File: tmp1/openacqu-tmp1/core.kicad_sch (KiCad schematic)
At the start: 35 parts, among them J1 GSB1C41110SSHR, J2 Test Points, U1 MCP2221AT-I_ML, U2 LP5817DRLR, U3 FXL6408UMX, U4 24AA025E48T-E_OT, U5 AP2112K-3.3TRG1, U6 TPS22996HQDYCRQ1

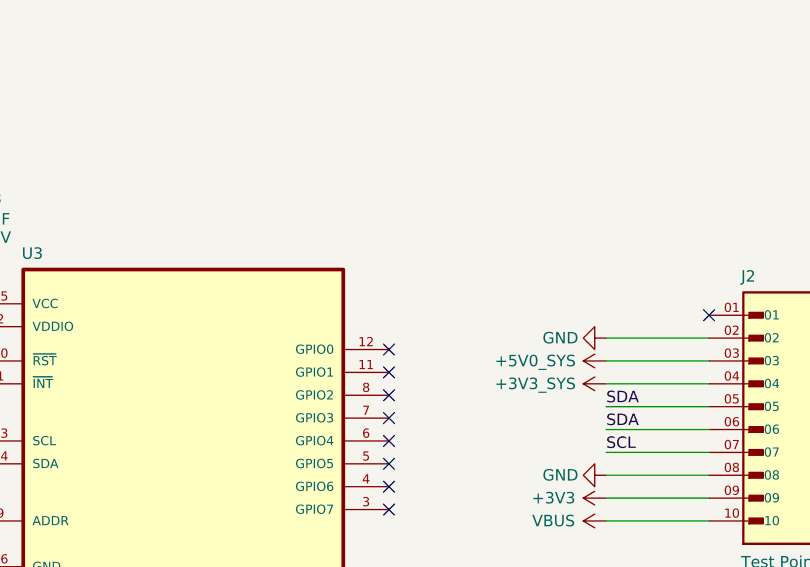
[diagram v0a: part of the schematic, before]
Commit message: Completed layout for the TMP1
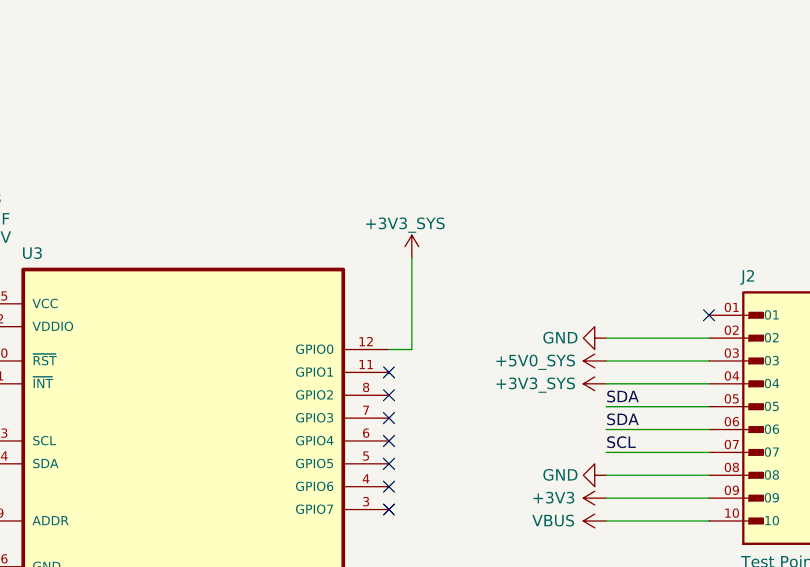
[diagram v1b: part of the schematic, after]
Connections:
- net +3V3_SYS: now also U3.12 (GPIO0)
- no-connect marks 19 -> 18
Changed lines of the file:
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@@
 	)
 	(no_connect
-		(at 229.87 110.49)
-	)
-	(no_connect
 		(at 69.85 124.46)
 	)
@@
 	(wire
 		(pts
+			(xy 232.41 110.49) (xy 229.87 110.49)
+		)
+		(stroke
+			(width 0)
+			(type default)
+		)
+	)
+	(wire
+		(pts
 			(xy 31.75 165.1) (xy 31.75 152.4)
 		)
@@
 	(wire
 		(pts
+			(xy 232.41 110.49) (xy 232.41 100.33)
+		)
+		(stroke
+			(width 0)
+			(type default)
+		)
+	)
+	(wire
+		(pts
 			(xy 168.91 111.76) (xy 168.91 114.3)
 		)
@@
 					(unit 1)
 				)
+			)
+		)
+	)
+	(symbol
+		(lib_id "power:+3V3")
+		(at 232.41 100.33 0)
+		(unit 1)
+		(exclude_from_sim no)
+		(in_bom yes)
+		(on_board yes)
+		(dnp no)
+		(property "Reference" "#PWR047"
+			(at 232.41 104.14 0)
+			(effects
+				(font
+					(size 1.27 1.27)
+				)
+				(hide yes)
+			)
+		)
+		(property "Value" "+3V3_SYS"
+			(at 231.648 96.52 0)
+			(effects
+				(font
+					(size 1.27 1.27)
+				)
+			)
+		)
+		(property "Footprint" ""
+			(at 232.41 100.33 0)
+			(effects
+				(font
+					(size 1.27 1.27)
+				)
+				(hide yes)
+			)
+		)
+		(property "Datasheet" ""
+			(at 232.41 100.33 0)
+			(effects
+				(font
+					(size 1.27 1.27)
+				)
+				(hide yes)
+			)
+		)
+		(property "Description" "Power symbol creates a global label with name \"+3V3\""
+			(at 232.41 100.33 0)
+			(effects
+				(font
+					(size 1.27 1.27)
+				)
+				(hide yes)
+			)
+		)
+		(pin "1"
+		)
+		(instances
+			(project "openacqu-tmp1"
+				(path "/2621f8e5-8f03-4409-8fc3-1378e1ab4580/64012f12-ce7d-4486-90ac-546df24347cc"
+					(reference "#PWR047")
+					(unit 1)
+				)

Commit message: Updated symbols with JLCPCB part numbers
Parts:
- C1, C2, C3, C4, C5, C6, C7, C8, C9: JLCPN (none) -> C29266
- D1: JLCPN (none) -> C5342281
- D2, D4: JLCPN (none) -> C2868952
- D3: JLCPN (none) -> C19725076
- J1: JLCPN (none) -> C34260841
- J2: now left out of the parts list
- R1, R2, R7, R8: JLCPN (none) -> C105872
- R10, R3, R4, R5, R6, R9: JLCPN (none) -> C851848
- U1: JLCPN (none) -> C623181
- U2: JLCPN (none) -> C47262829
- U3: JLCPN (none) -> C457770
- U4: JLCPN (none) -> C2066000
- U5: JLCPN (none) -> C51118
- U6: JLCPN (none) -> C43131299
